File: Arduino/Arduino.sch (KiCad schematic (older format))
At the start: 9 parts, among them P1 Power, P2 Analog, P3 Digital, P4 Digital, P5 CONN_01X01, P6 CONN_01X01, P7 CONN_01X01, P8 CONN_01X01

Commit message: Add 16 crystal
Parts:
- added Y?: 16MHz, Crystals:Crystal_SMD_3225-4pin_3.2x2.5mm, symbol Device:Crystal_GND24
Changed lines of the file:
@@
+	1    0    0    -1
+$EndComp
+$Comp
+L Device:Crystal_GND24 Y?
+U 1 1 5FF3BE14
+P 7550 4750
+F 0 "Y?" H 7650 4950 50  0000 L CNN
+F 1 "16MHz" H 7650 4550 50  0000 L CNN
+F 2 "Crystals:Crystal_SMD_3225-4pin_3.2x2.5mm" H 7550 4750 50  0001 C CNN
+F 3 "https://datasheet.lcsc.com/szlcsc/Yangxing-Tech-X322516MLB4SI_C13738.pdf" H 7550 4750 50  0001 C CNN
+F 4 "" H 7550 4750 50  0001 C CNN "Digikey"
+F 5 "C13738" H 7550 4750 50  0001 C CNN "JLC"
+	1    7550 4750
 	1    0    0    -1
 $EndComp

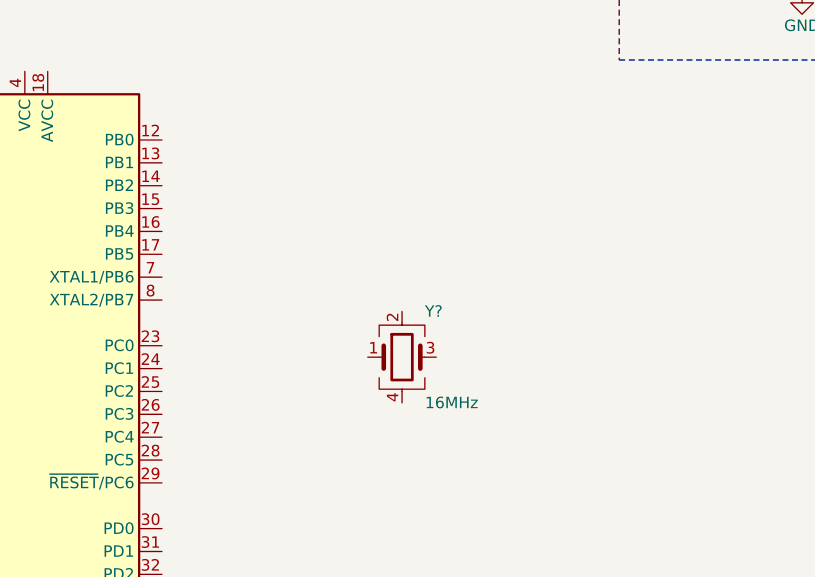
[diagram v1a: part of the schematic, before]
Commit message: add capacitors for crystal
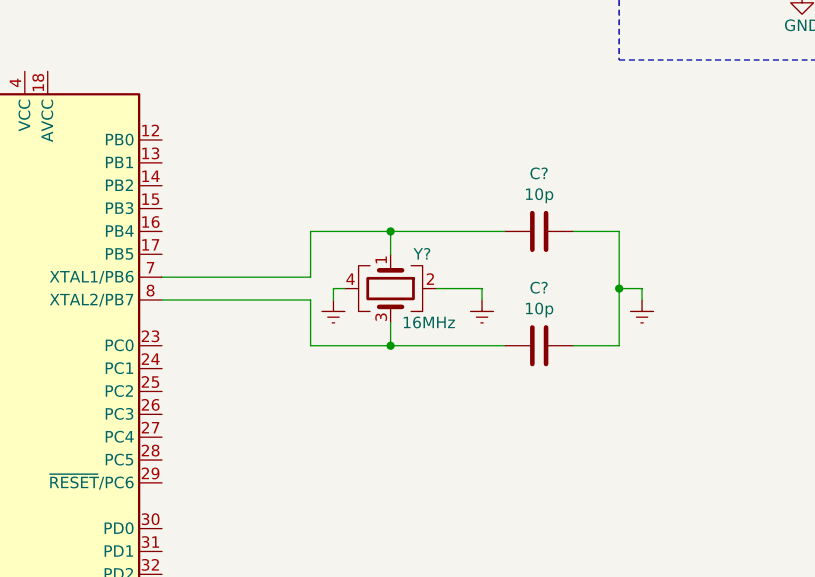
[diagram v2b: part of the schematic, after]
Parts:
- added C? (x2): 10p, Capacitors_SMD:C_0402, symbol Device:C
- Y?: MFR (none) -> X322516MLB4SI
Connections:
- net at U?.7 (XTAL1/PB6): now also Y?.1, C?.2
- net at U?.8 (XTAL2/PB7): now also Y?.3, C?.2
- net GNDREF: now reaches Y?.2
- net GNDREF: now also Y?.4, C?.1, C?.1
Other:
- moved on the sheet: Y?
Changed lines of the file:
@@
 L Device:Crystal_GND24 Y?
 U 1 1 5FF3BE14
-P 7550 4750
-F 0 "Y?" H 7650 4950 50  0000 L CNN
-F 1 "16MHz" H 7650 4550 50  0000 L CNN
-F 2 "Crystals:Crystal_SMD_3225-4pin_3.2x2.5mm" H 7550 4750 50  0001 C CNN
-F 3 "https://datasheet.lcsc.com/szlcsc/Yangxing-Tech-X322516MLB4SI_C13738.pdf" H 7550 4750 50  0001 C CNN
-F 4 "" H 7550 4750 50  0001 C CNN "Digikey"
-F 5 "C13738" H 7550 4750 50  0001 C CNN "JLC"
-	1    7550 4750
+P 7500 4450
+F 0 "Y?" V 7350 4550 50  0000 L CNN
+F 1 "16MHz" V 7650 4500 50  0000 L CNN
+F 2 "Crystals:Crystal_SMD_3225-4pin_3.2x2.5mm" H 7500 4450 50  0001 C CNN
+F 3 "https://datasheet.lcsc.com/szlcsc/Yangxing-Tech-X322516MLB4SI_C13738.pdf" H 7500 4450 50  0001 C CNN
+F 4 "" H 7500 4450 50  0001 C CNN "Digikey"
+F 5 "C13738" H 7500 4450 50  0001 C CNN "JLC"
+F 6 "X322516MLB4SI" V 7500 4450 50  0001 C CNN "MFR"
+	1    7500 4450
+	0    1    1    0
+$EndComp
+Wire Wire Line
+	6500 4400 7150 4400
+Wire Wire Line
+	7150 4400 7150 4200
+Wire Wire Line
+	7150 4200 7500 4200
+Wire Wire Line
+	7500 4200 7500 4300
+Wire Wire Line
+	6500 4500 7150 4500
+Wire Wire Line
+	7150 4500 7150 4700
+Wire Wire Line
+	7150 4700 7500 4700
+Wire Wire Line
+	7500 4700 7500 4600
+$Comp
+L Device:C C?
+U 1 1 5FF593A8
+P 8150 4200
+F 0 "C?" V 7898 4200 50  0000 C CNN
+F 1 "10p" V 7989 4200 50  0000 C CNN
+F 2 "Capacitors_SMD:C_0402" H 8188 4050 50  0001 C CNN
+F 3 "https://datasheet.lcsc.com/szlcsc/Samsung-Electro-Mechanics-CL05C100JB5NNNC_C32949.pdf" H 8150 4200 50  0001 C CNN
+F 4 "1276-1139-1-ND" H 8150 4200 50  0001 C CNN "Digikey"
+F 5 "C32949" H 8150 4200 50  0001 C CNN "JLC"
+F 6 "CL05C100JB5NNNC" H 8150 4200 50  0001 C CNN "MFR"
+	1    8150 4200
+	0    1    1    0
+$EndComp
+$Comp
+L power:GNDREF #PWR?
+U 1 1 5FF59D95
+P 7250 4500
+F 0 "#PWR?" H 7250 4250 50  0001 C CNN
+F 1 "GNDREF" H 7255 4327 50  0001 C CNN
+F 2 "" H 7250 4500 50  0001 C CNN
+F 3 "" H 7250 4500 50  0001 C CNN
+	1    7250 4500
 	1    0    0    -1
 $EndComp
+Wire Wire Line
+	7250 4500 7250 4450
+Wire Wire Line
+	7250 4450 7300 4450
+$Comp
+L power:GNDREF #PWR?
+U 1 1 5FF5BAEC
+P 7900 4500
+F 0 "#PWR?" H 7900 4250 50  0001 C CNN
+F 1 "GNDREF" H 7905 4327 50  0001 C CNN
+F 2 "" H 7900 4500 50  0001 C CNN
+F 3 "" H 7900 4500 50  0001 C CNN
+	1    7900 4500
+	1    0    0    -1
+$EndComp
+Wire Wire Line
+	7700 4450 7900 4450
+Wire Wire Line
+	7900 4450 7900 4500
+Wire Wire Line
+	7500 4200 8000 4200
+Connection ~ 7500 4200
+$Comp
+L Device:C C?
+U 1 1 5FF5F758
+P 8150 4700
+F 0 "C?" V 7898 4700 50  0000 C CNN
+F 1 "10p" V 7989 4700 50  0000 C CNN
+F 2 "Capacitors_SMD:C_0402" H 8188 4550 50  0001 C CNN
+F 3 "https://datasheet.lcsc.com/szlcsc/Samsung-Electro-Mechanics-CL05C100JB5NNNC_C32949.pdf" H 8150 4700 50  0001 C CNN
+F 4 "1276-1139-1-ND" H 8150 4700 50  0001 C CNN "Digikey"
+F 5 "C32949" H 8150 4700 50  0001 C CNN "JLC"
+F 6 "CL05C100JB5NNNC" H 8150 4700 50  0001 C CNN "MFR"
+	1    8150 4700
+	0    1    1    0
+$EndComp
+Wire Wire Line
+	8000 4700 7500 4700
+Connection ~ 7500 4700
+Wire Wire Line
+	8300 4200 8500 4200
+Wire Wire Line
+	8500 4200 8500 4450
+Wire Wire Line
+	8500 4700 8300 4700
+Wire Wire Line
+	8500 4450 8600 4450
+Wire Wire Line
+	8600 4450 8600 4500
+Connection ~ 8500 4450
+Wire Wire Line
+	8500 4450 8500 4700
+$Comp
+L power:GNDREF #PWR?
+U 1 1 5FF64ED6
+P 8600 4500
+F 0 "#PWR?" H 8600 4250 50  0001 C CNN
+F 1 "GNDREF" H 8605 4327 50  0001 C CNN
+F 2 "" H 8600 4500 50  0001 C CNN
+F 3 "" H 8600 4500 50  0001 C CNN
+	1    8600 4500
+	1    0    0    -1
+$EndComp

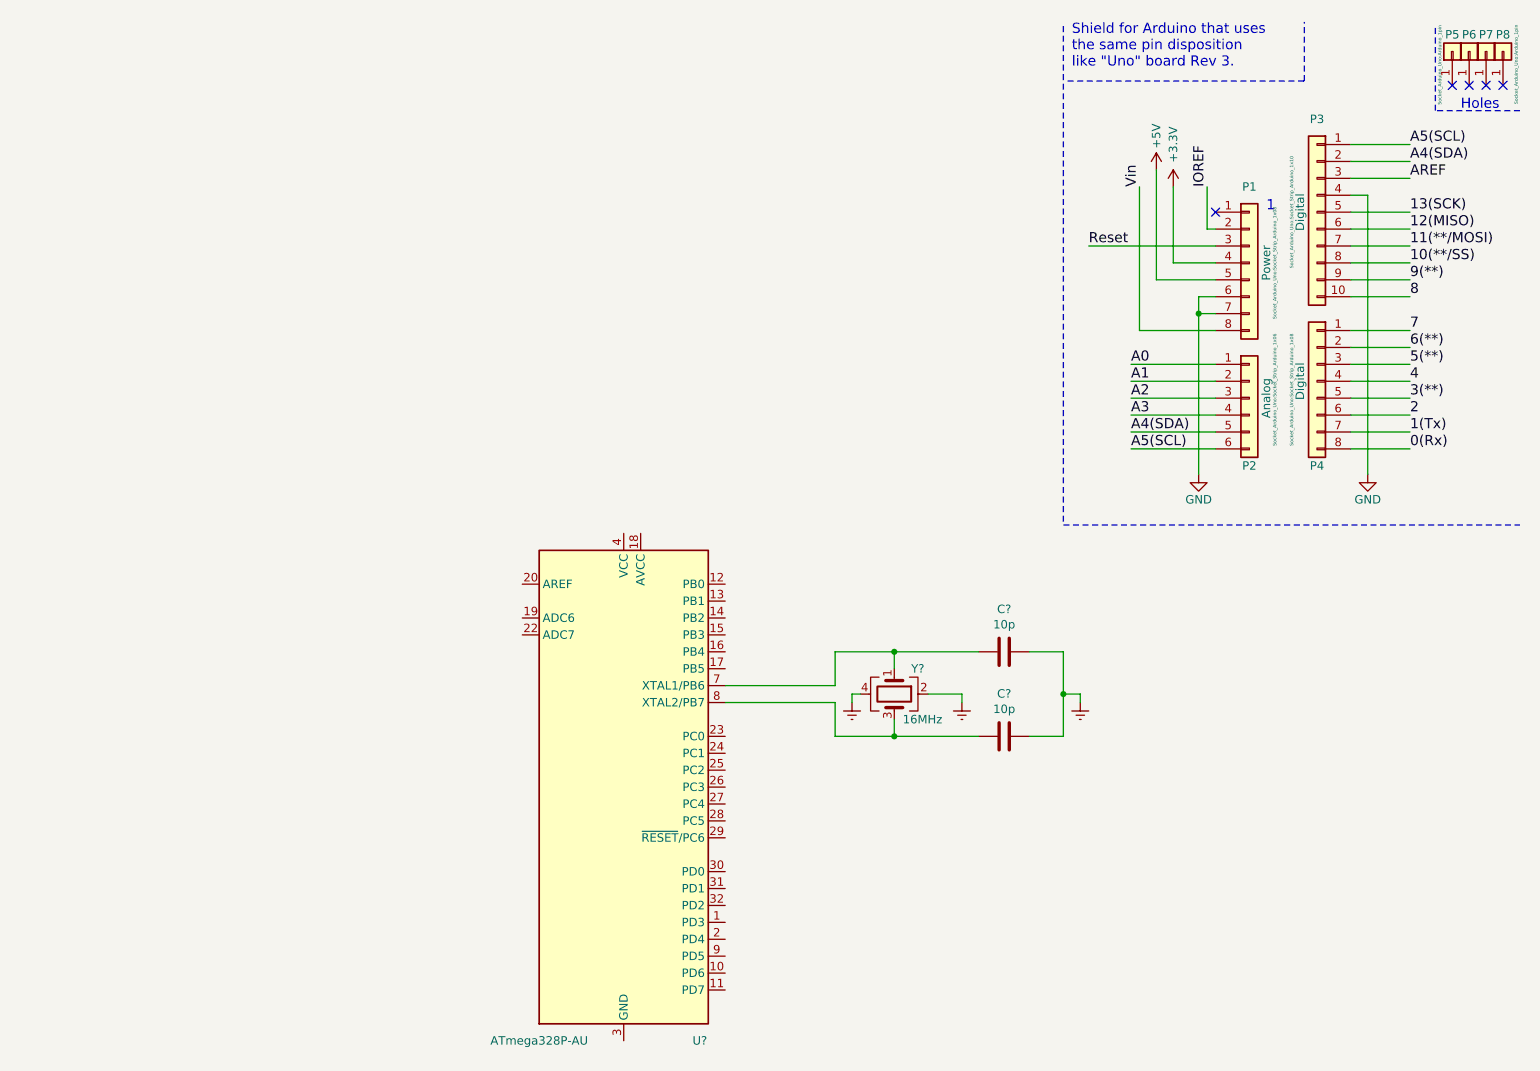
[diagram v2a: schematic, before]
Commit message: connect pin to MCU
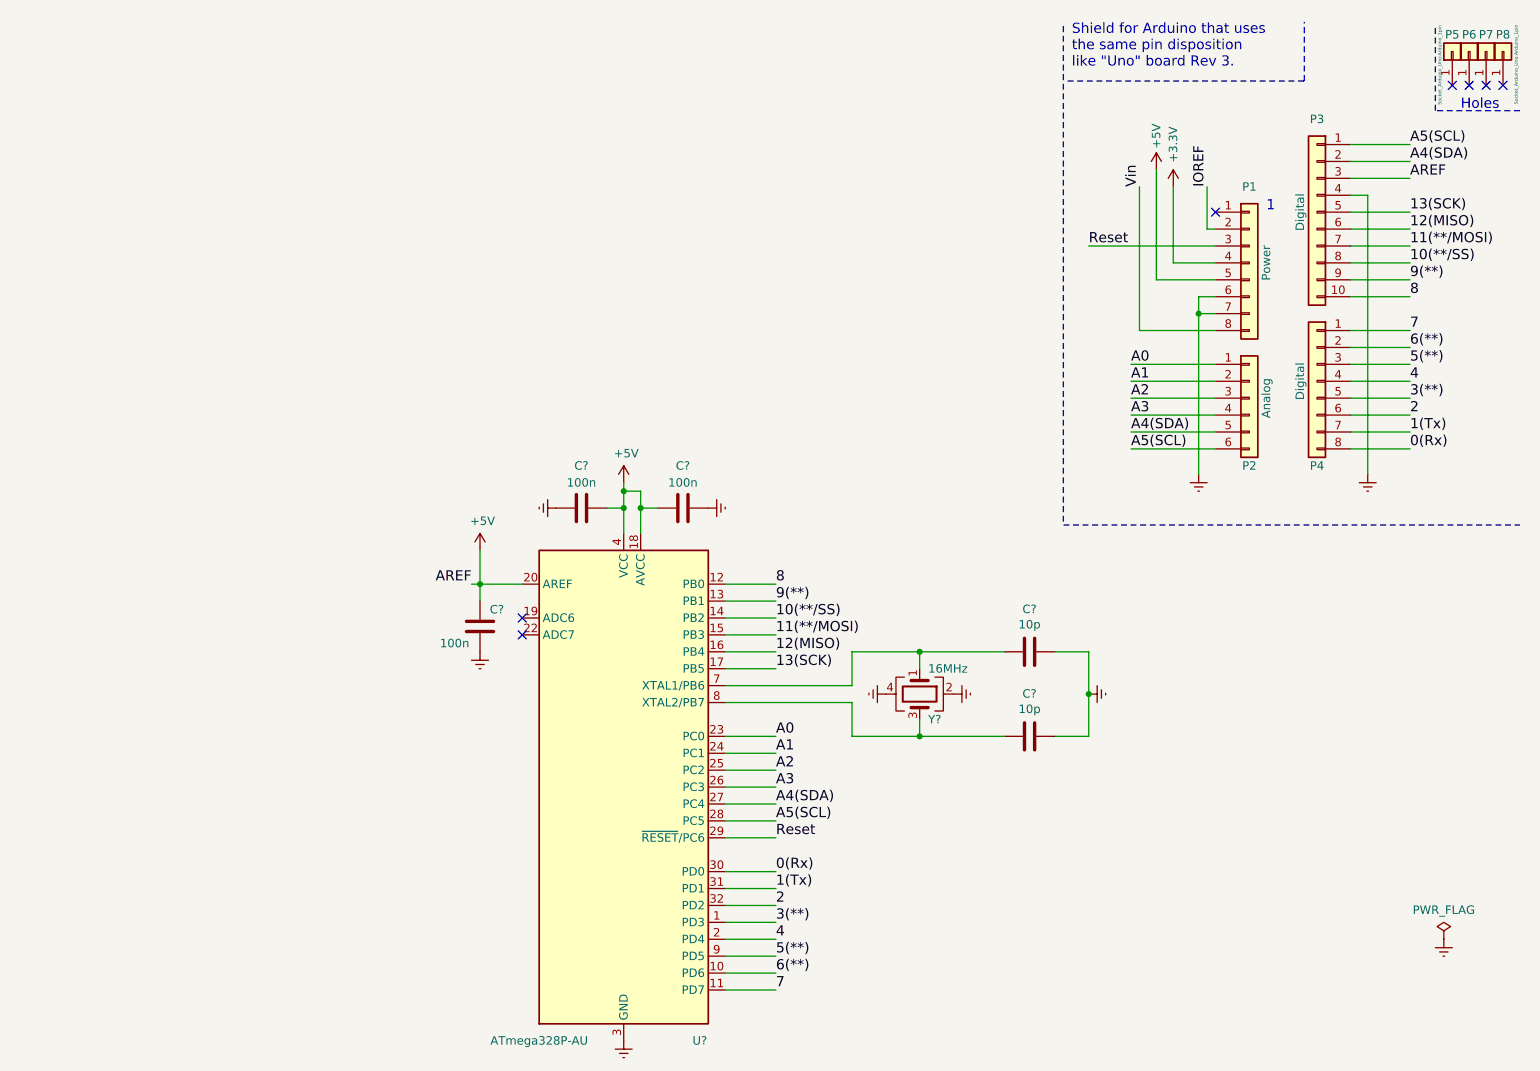
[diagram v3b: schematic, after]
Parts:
- added C? (x3): 100n, Capacitors_SMD:C_0402, symbol Device:C
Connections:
- net AREF is gone; now on net +5V: P3.3 (Pin_3)
- net GND is gone; now on net GNDREF: P1.6 (Pin_6), P1.7 (Pin_7), P3.4 (Pin_4)
- net +5V: now also U?.18 (AVCC), U?.20 (AREF), U?.4 (VCC), U?.6 (VCC), C?.1, C?.1, C?.2
- net 0(Rx): now also U?.30 (PD0)
- net 1(Tx): now also U?.31 (PD1)
- net 10(**/SS): now also U?.14 (PB2)
- net 11(**/MOSI): now also U?.15 (PB3)
- net 12(MISO): now also U?.16 (PB4)
- net 13(SCK): now also U?.17 (PB5)
- net 2: now also U?.32 (PD2)
- net 3(**): now also U?.1 (PD3)
- net 4: now also U?.2 (PD4)
- net 5(**): now also U?.9 (PD5)
- net 6(**): now also U?.10 (PD6)
- net 7: now also U?.11 (PD7)
- net 8: now also U?.12 (PB0)
- net 9(**): now also U?.13 (PB1)
- net A0: now also U?.23 (PC0)
- net A1: now also U?.24 (PC1)
- net A2: now also U?.25 (PC2)
- net A3: now also U?.26 (PC3)
- net A4(SDA): now also U?.27 (PC4)
- net A5(SCL): now also U?.28 (PC5)
- net GNDREF: now also U?.21 (GND), U?.3 (GND), U?.5 (GND), C?.1, C?.2, C?.2
- net Reset: now also U?.29 (~RESET~/PC6)
- no-connect marks 5 -> 7
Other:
- moved on the sheet: C?, Y?

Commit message: Add linear regulator
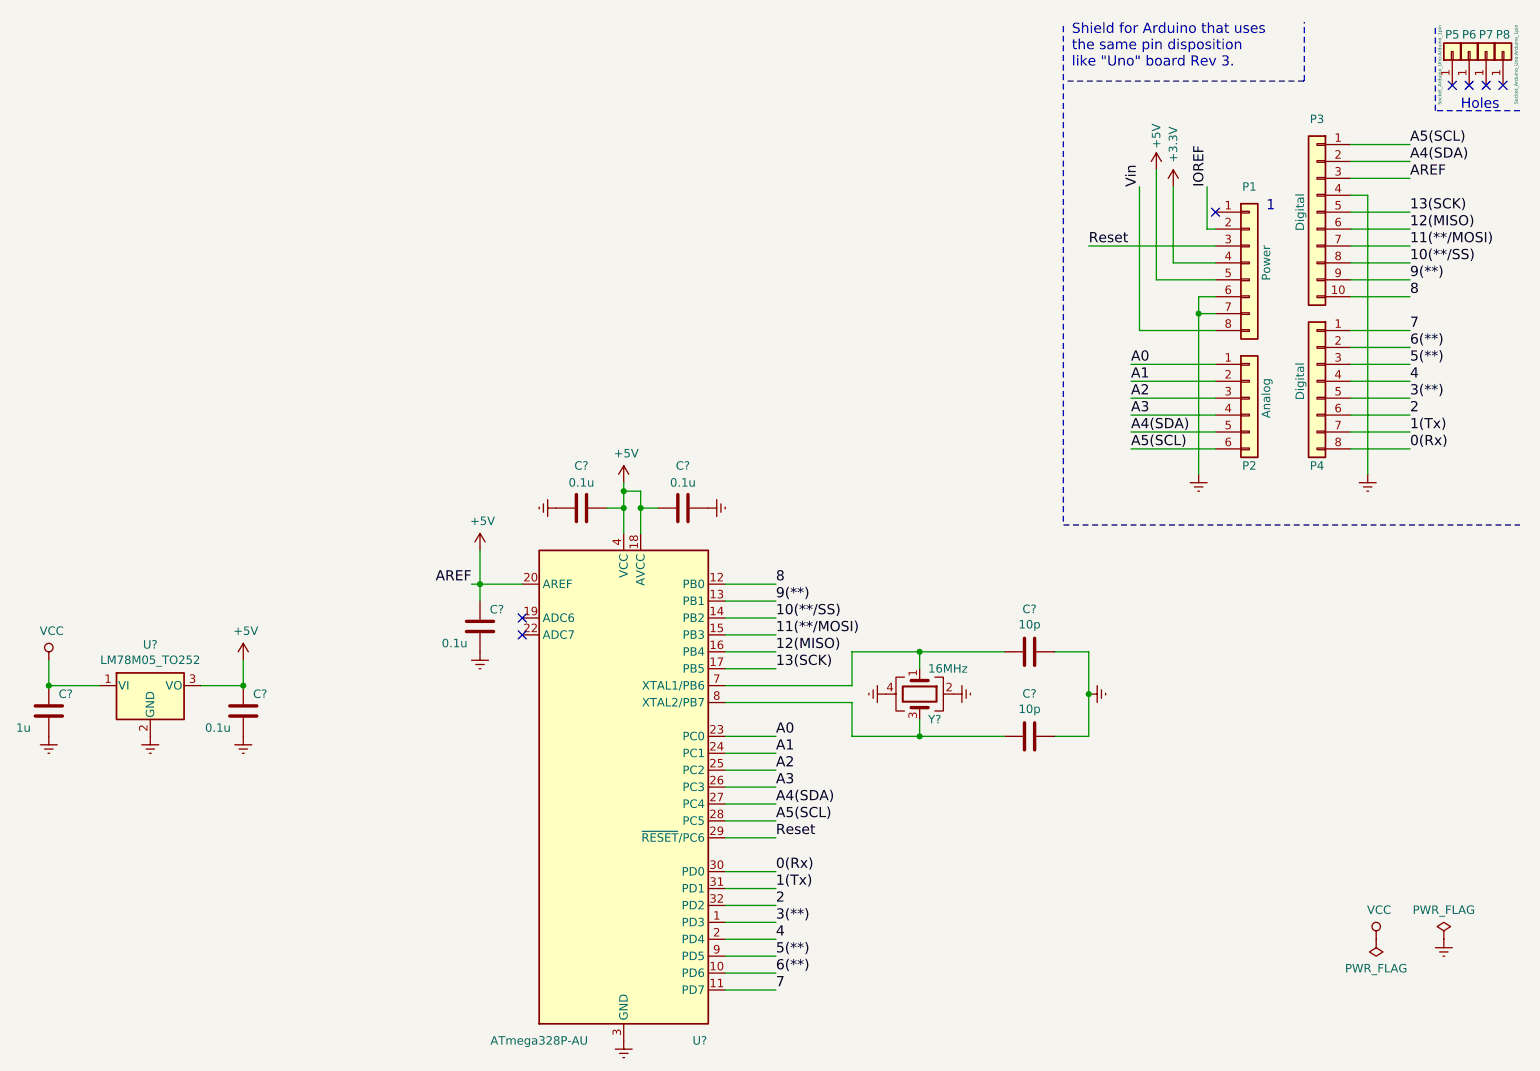
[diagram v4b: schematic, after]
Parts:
- added C?: 0.1u, Capacitors_SMD:C_0402, symbol Device:C
- added C?: 1u, Capacitors_SMD:C_0402, symbol Device:C
- added U?: LM78M05_TO252, TO_SOT_Packages_SMD:TO-252-2, symbol Regulator_Linear:LM78M05_TO252
- C? (x3): value 100n -> 0.1u
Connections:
- net +5V: now also C?.1, U?.3 (VO)
- net GNDREF: now also C?.2, C?.2, U?.2 (GND)
- new net VCC: C?.1, U?.1 (VI)
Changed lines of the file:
@@
 P 5050 4050
 F 0 "C?" H 5150 4150 50  0000 C CNN
-F 1 "100n" H 4900 3950 50  0000 C CNN
+F 1 "0.1u" H 4900 3950 50  0000 C CNN
 F 2 "Capacitors_SMD:C_0402" H 5088 3900 50  0001 C CNN
 F 3 "https://datasheet.lcsc.com/szlcsc/Samsung-Electro-Mechanics-CL05C100JB5NNNC_C32949.pdf" H 5050 4050 50  0001 C CNN
@@
 P 6250 3350
 F 0 "C?" V 6000 3350 50  0000 C CNN
-F 1 "100n" V 6100 3350 50  0000 C CNN
+F 1 "0.1u" V 6100 3350 50  0000 C CNN
 F 2 "Capacitors_SMD:C_0402" H 6288 3200 50  0001 C CNN
 F 3 "https://datasheet.lcsc.com/szlcsc/Samsung-Electro-Mechanics-CL05C100JB5NNNC_C32949.pdf" H 6250 3350 50  0001 C CNN
@@
 P 5650 3350
 F 0 "C?" V 5400 3350 50  0000 C CNN
-F 1 "100n" V 5500 3350 50  0000 C CNN
+F 1 "0.1u" V 5500 3350 50  0000 C CNN
 F 2 "Capacitors_SMD:C_0402" H 5688 3200 50  0001 C CNN
 F 3 "https://datasheet.lcsc.com/szlcsc/Samsung-Electro-Mechanics-CL05C100JB5NNNC_C32949.pdf" H 5650 3350 50  0001 C CNN
@@
 Text Label 10550 1400 0    60   ~ 0
 AREF
+$Comp
+L Regulator_Linear:LM78M05_TO252 U?
+U 1 1 6000EF14
+P 3100 4400
+F 0 "U?" H 3100 4642 50  0000 C CNN
+F 1 "LM78M05_TO252" H 3100 4551 50  0000 C CNN
+F 2 "TO_SOT_Packages_SMD:TO-252-2" H 3100 4625 50  0001 C CIN
+F 3 "https://datasheet.lcsc.com/szlcsc/STMicroelectronics-L78M05ABDT-TR_C58069.pdf" H 3100 4350 50  0001 C CNN
+F 4 "497-1201-1-ND" H 3100 4400 50  0001 C CNN "Digikey"
+F 5 "C75510" H 3100 4400 50  0001 C CNN "LSC"
+F 6 "L78M05ABDT-TR" H 3100 4400 50  0001 C CNN "MFR"
+	1    3100 4400
+	1    0    0    -1
+$EndComp
+Wire Wire Line
+	2800 4400 2500 4400
+Wire Wire Line
+	2500 4400 2500 4250
+$Comp
+L power:VCC #PWR?
+U 1 1 60014ACC
+P 2500 4250
+F 0 "#PWR?" H 2500 4100 50  0001 C CNN
+F 1 "VCC" H 2517 4423 50  0000 C CNN
+F 2 "" H 2500 4250 50  0001 C CNN
+F 3 "" H 2500 4250 50  0001 C CNN
+	1    2500 4250
+	1    0    0    -1
+$EndComp
+$Comp
+L power:VCC #PWR?
+U 1 1 60015652
+P 10350 5900
+F 0 "#PWR?" H 10350 5750 50  0001 C CNN
+F 1 "VCC" H 10367 6073 50  0000 C CNN
+F 2 "" H 10350 5900 50  0001 C CNN
+F 3 "" H 10350 5900 50  0001 C CNN
+	1    10350 5900
+	1    0    0    -1
+$EndComp
+$Comp
+L power:PWR_FLAG #FLG?
+U 1 1 600160A3
+P 10350 5900
+F 0 "#FLG?" H 10350 5975 50  0001 C CNN
+F 1 "PWR_FLAG" H 10350 6073 50  0000 C CNN
+F 2 "" H 10350 5900 50  0001 C CNN
+F 3 "~" H 10350 5900 50  0001 C CNN
+	1    10350 5900
+	-1   0    0    1
+$EndComp
+$Comp
+L power:GNDREF #PWR?
+U 1 1 60016A9F
+P 3100 4700
+F 0 "#PWR?" H 3100 4450 50  0001 C CNN
+F 1 "GNDREF" H 3105 4527 50  0001 C CNN
+F 2 "" H 3100 4700 50  0001 C CNN
+F 3 "" H 3100 4700 50  0001 C CNN
+	1    3100 4700
+	1    0    0    -1
+$EndComp
+$Comp
+L power:+5V #PWR?
+U 1 1 6001743C
+P 3650 4250
+F 0 "#PWR?" H 3650 4100 50  0001 C CNN
+F 1 "+5V" H 3665 4423 50  0000 C CNN
+F 2 "" H 3650 4250 50  0001 C CNN
+F 3 "" H 3650 4250 50  0001 C CNN
+	1    3650 4250
+	1    0    0    -1
+$EndComp
+Wire Wire Line
+	3400 4400 3650 4400
+Wire Wire Line
+	3650 4400 3650 4250
+$Comp
+L power:GNDREF #PWR?
+U 1 1 60020F46
+P 3650 4700
+F 0 "#PWR?" H 3650 4450 50  0001 C CNN
+F 1 "GNDREF" H 3655 4527 50  0001 C CNN
+F 2 "" H 3650 4700 50  0001 C CNN
+F 3 "" H 3650 4700 50  0001 C CNN
+	1    3650 4700
+	1    0    0    -1
+$EndComp
+$Comp
+L Device:C C?
+U 1 1 60024AFE
+P 3650 4550
+F 0 "C?" H 3750 4650 50  0000 C CNN
+F 1 "0.1u" H 3500 4450 50  0000 C CNN
+F 2 "Capacitors_SMD:C_0402" H 3688 4400 50  0001 C CNN
+F 3 "https://datasheet.lcsc.com/szlcsc/Samsung-Electro-Mechanics-CL05C100JB5NNNC_C32949.pdf" H 3650 4550 50  0001 C CNN
+F 4 "1276-1001-1-ND" H 3650 4550 50  0001 C CNN "Digikey"
+F 5 "C1525" H 3650 4550 50  0001 C CNN "JLC"
+F 6 "CL05B104KO5NNNC" H 3650 4550 50  0001 C CNN "MFR"
+	1    3650 4550
+	1    0    0    -1
+$EndComp
+Connection ~ 3650 4400
+$Comp
+L Device:C C?
+U 1 1 6002548C
+P 2500 4550
+F 0 "C?" H 2600 4650 50  0000 C CNN
+F 1 "1u" H 2350 4450 50  0000 C CNN
+F 2 "Capacitors_SMD:C_0402" H 2538 4400 50  0001 C CNN
+F 3 "https://datasheet.lcsc.com/szlcsc/Samsung-Electro-Mechanics-CL05C100JB5NNNC_C32949.pdf" H 2500 4550 50  0001 C CNN
+F 4 "" H 2500 4550 50  0001 C CNN "Digikey"
+F 5 "C52923" H 2500 4550 50  0001 C CNN "JLC"
+F 6 "CL05A105KA5NQNC" H 2500 4550 50  0001 C CNN "MFR"
+	1    2500 4550
+	1    0    0    -1
+$EndComp
+Connection ~ 2500 4400
+$Comp
+L power:GNDREF #PWR?
+U 1 1 60025922
+P 2500 4700
+F 0 "#PWR?" H 2500 4450 50  0001 C CNN
+F 1 "GNDREF" H 2505 4527 50  0001 C CNN
+F 2 "" H 2500 4700 50  0001 C CNN
+F 3 "" H 2500 4700 50  0001 C CNN
+	1    2500 4700
+	1    0    0    -1
+$EndComp
 $EndSCHEMATC
